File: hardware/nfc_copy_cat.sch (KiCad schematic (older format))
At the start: 28 parts, among them J1 USB_B_Micro, J2 Screw_Terminal_01x02, J3 Conn_02x02_Counter_Clockwise, J4 Conn_01x08, J5 Conn_01x02, J6 Conn_01x04, SW1 SW_DPST_x2, SW2 SW_DPST_x2, SW3 SW_DPST_x2, U1 AP2112K-3.3TRG1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

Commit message: añadimiento de led
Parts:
- added D4: LED_Small, LED_SMD:LED_0805_2012Metric_Pad1.15x1.40mm_HandSolder, symbol Device:LED_Small
- added R4: 330, Resistor_SMD:R_0805_2012Metric_Pad1.15x1.40mm_HandSolder, symbol Device:R_Small
- C4: value 0.1UF -> 0.1uf
- C6, C7, C8: value C -> 10uf
- R2: value R -> 1k
- R3: value R -> 2.2k
- U1: symbol croketa:AP2112K-3.3TRG1 -> electroniccats:AP2112K-3.3TRG1
- renumbered c1 to C1, c3 to C3
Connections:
- net labels added: 2(LED)
- wire segments 75 -> 78
- no-connect marks 21 -> 20
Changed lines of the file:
@@
 EESchema Schematic File Version 4
-LIBS:placa inventors house 1-cache
+LIBS:nfc_copy_cat-cache
 EELAYER 29 0
 EELAYER END
@@
 P 10800 1230
 F 0 "C4" H 10892 1276 50  0000 L CNN
-F 1 "0.1UF" H 10892 1185 50  0000 L CNN
+F 1 "0.1uf" H 10892 1185 50  0000 L CNN
 F 2 "Capacitor_SMD:C_0805_2012Metric_Pad1.15x1.40mm_HandSolder" H 10800 1230 50  0001 C CNN
 F 3 "~" H 10800 1230 50  0001 C CNN
@@
 	4950 1920 4950 1970
 $Comp
-L Device:C_Small c3
+L Device:C_Small C3
 U 1 1 5D106941
 P 4250 2070
-F 0 "c3" H 4342 2116 50  0000 L CNN
+F 0 "C3" H 4342 2116 50  0000 L CNN
 F 1 "0.1uf" H 4342 2025 50  0000 L CNN
 F 2 "Capacitor_SMD:C_0805_2012Metric_Pad1.15x1.40mm_HandSolder" H 4250 2070 50  0001 C CNN
@@
 $EndComp
 $Comp
-L Device:C_Small c1
+L Device:C_Small C1
 U 1 1 5D1030E9
 P 4950 2070
-F 0 "c1" H 5042 2116 50  0000 L CNN
+F 0 "C1" H 5042 2116 50  0000 L CNN
 F 1 "0.1uf" H 5042 2025 50  0000 L CNN
 F 2 "Capacitor_SMD:C_0805_2012Metric_Pad1.15x1.40mm_HandSolder" H 4950 2070 50  0001 C CNN
@@
 P 2310 3560
 F 0 "R2" H 2380 3606 50  0000 L CNN
-F 1 "R" H 2380 3515 50  0000 L CNN
+F 1 "1k" H 2380 3515 50  0000 L CNN
 F 2 "Resistor_SMD:R_0805_2012Metric_Pad1.15x1.40mm_HandSolder" V 2240 3560 50  0001 C CNN
 F 3 "~" H 2310 3560 50  0001 C CNN
@@
 P 1150 4020
 F 0 "R3" V 1357 4020 50  0000 C CNN
-F 1 "R" V 1266 4020 50  0000 C CNN
+F 1 "2.2k" V 1266 4020 50  0000 C CNN
 F 2 "Resistor_SMD:R_0805_2012Metric_Pad1.15x1.40mm_HandSolder" V 1080 4020 50  0001 C CNN
 F 3 "~" H 1150 4020 50  0001 C CNN
@@
 P 2180 4400
 F 0 "C7" H 2295 4446 50  0000 L CNN
-F 1 "C" H 2295 4355 50  0000 L CNN
+F 1 "10uf" H 2295 4355 50  0000 L CNN
 F 2 "Capacitor_SMD:C_0805_2012Metric_Pad1.15x1.40mm_HandSolder" H 2218 4250 50  0001 C CNN
 F 3 "~" H 2180 4400 50  0001 C CNN
@@
 P 910 3550
 F 0 "C8" H 1025 3596 50  0000 L CNN
-F 1 "C" H 1025 3505 50  0000 L CNN
+F 1 "10uf" H 1025 3505 50  0000 L CNN
 F 2 "Capacitor_SMD:C_0805_2012Metric_Pad1.15x1.40mm_HandSolder" H 948 3400 50  0001 C CNN
 F 3 "~" H 910 3550 50  0001 C CNN
@@
 NoConn ~ 7500 3620
 NoConn ~ 7500 3720
-NoConn ~ 7500 2720
 NoConn ~ 7500 2820
 NoConn ~ 10380 2480
@@
 $EndComp
 $Comp
-L croketa:AP2112K-3.3TRG1 U1
+L electroniccats:AP2112K-3.3TRG1 U1
 U 1 1 5D11FC1B
 P 1690 2450
@@
 P 2440 2400
 F 0 "C6" H 2555 2446 50  0000 L CNN
-F 1 "C" H 2555 2355 50  0000 L CNN
+F 1 "10uf" H 2555 2355 50  0000 L CNN
 F 2 "Capacitor_SMD:C_0805_2012Metric_Pad1.15x1.40mm_HandSolder" H 2478 2250 50  0001 C CNN
 F 3 "~" H 2440 2400 50  0001 C CNN
@@
 NoConn ~ 10320 4520
 NoConn ~ 10320 4420
+Wire Bus Line
+	3300 1830 3930 1830
+Wire Bus Line
+	3930 1830 3930 470
+$Comp
+L Device:LED_Small D4
+U 1 1 5D36129D
+P 3720 1220
+F 0 "D4" V 3766 1152 50  0000 R CNN
+F 1 "LED_Small" V 3675 1152 50  0000 R CNN
+F 2 "LED_SMD:LED_0805_2012Metric_Pad1.15x1.40mm_HandSolder" V 3720 1220 50  0001 C CNN
+F 3 "~" V 3720 1220 50  0001 C CNN
+	1    3720 1220
+	0    1    1    0
+$EndComp
+$Comp
+L Device:R_Small R4
+U 1 1 5D3612A3
+P 3720 970
+F 0 "R4" H 3779 1016 50  0000 L CNN
+F 1 "330" H 3779 925 50  0000 L CNN
+F 2 "Resistor_SMD:R_0805_2012Metric_Pad1.15x1.40mm_HandSolder" H 3720 970 50  0001 C CNN
+F 3 "~" H 3720 970 50  0001 C CNN
+	1    3720 970
+	-1   0    0    1
+$EndComp
+$Comp
+L MagSpoofTC-cache:GND #PWR026
+U 1 1 5D3612A9
+P 3720 820
+F 0 "#PWR026" H 3720 570 50  0001 C CNN
+F 1 "GND" H 3725 647 50  0000 C CNN
+F 2 "" H 3720 820 50  0000 C CNN
+F 3 "" H 3720 820 50  0000 C CNN
+	1    3720 820
+	-1   0    0    1
+$EndComp
+Wire Wire Line
+	3720 1370 3720 1320
+Wire Wire Line
+	3720 1120 3720 1070
+Wire Wire Line
+	3720 870  3720 820
+Text Label 7500 2720 0    50   ~ 0
+2(LED)
+Text Label 3720 1370 2    50   ~ 0
+2(LED)
 $EndSCHEMATC

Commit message: update schematic
new connector swd, fix cap vddcore, add leds
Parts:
- removed C3: 0.1uf, Capacitor_SMD:C_0805_2012Metric_Pad1.15x1.40mm_HandSolder, symbol Device:C_Small
- removed J3: Conn_02x02_Counter_Clockwise, Connector_PinHeader_2.54mm:PinHeader_2x02_P2.54mm_Vertical_SMD, symbol Connector_Generic:Conn_02x02_Counter_Clockwise
- removed J6: Conn_01x04, Connector_PinHeader_2.54mm:PinHeader_1x04_P2.54mm_Vertical, symbol Connector_Generic:Conn_01x04
- added D5, D6: LED, LED_SMD:LED_0805_2012Metric_Pad1.15x1.40mm_HandSolder, symbol Device:LED_Small
- added J3: SWD, symbol Connector:Conn_01x04_Male
- added R5, R6: 330, Resistor_SMD:R_0805_2012Metric_Pad1.15x1.40mm_HandSolder, symbol Device:R_Small
- D1: value LED_Small -> POWER
- D2: value D_Schottky -> MBR120
- D4: value LED_Small -> LED
- J2: value Screw_Terminal_01x02 -> Battery
- SW1: value SW_DPST_x2 -> RST; symbol Switch:SW_DPST_x2 -> nfc_copy_cat-rescue:SW_DPST_x2-Switch
- SW2: value SW_DPST_x2 -> Magspoof; symbol Switch:SW_DPST_x2 -> nfc_copy_cat-rescue:SW_DPST_x2-Switch
- SW3: value SW_DPST_x2 -> NFC; symbol Switch:SW_DPST_x2 -> nfc_copy_cat-rescue:SW_DPST_x2-Switch
- U3: symbol MagSpoofTC-cache:TC4424 -> nfc_copy_cat-rescue:TC4424-MagSpoofTC-cache
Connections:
- net labels added: +BATT, LED1, LED2, LED3
- net labels removed: 2(LED)
- wire segments 78 -> 81
- no-connect marks 20 -> 14
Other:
- note added: "COIL"
- note added: "MICROCONTROLLER"
- note added: "NFC CONNECTOR"
- note added: "SOURCE AND CHARGER"
- moved on the sheet: C1, C2, C4, C5, C6, D1, D2, D4, J2, J4, J5, R1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

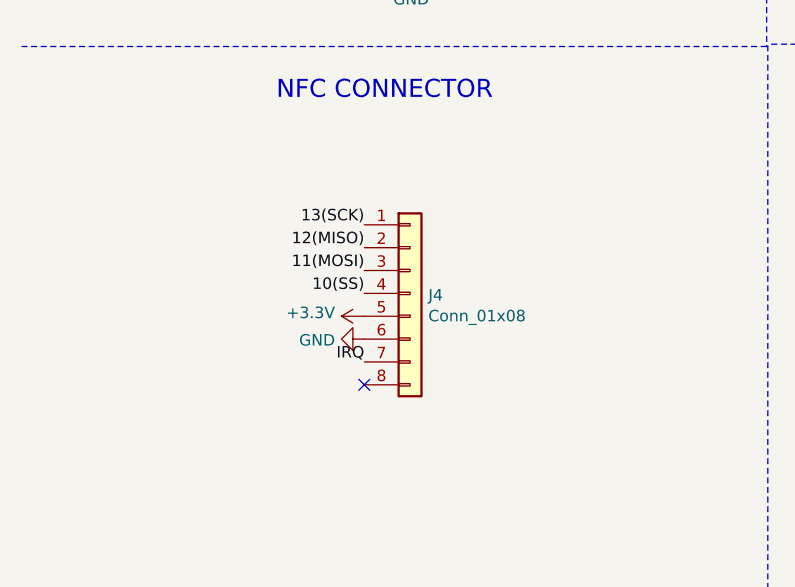
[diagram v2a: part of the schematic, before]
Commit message: add connector adafruit NFC
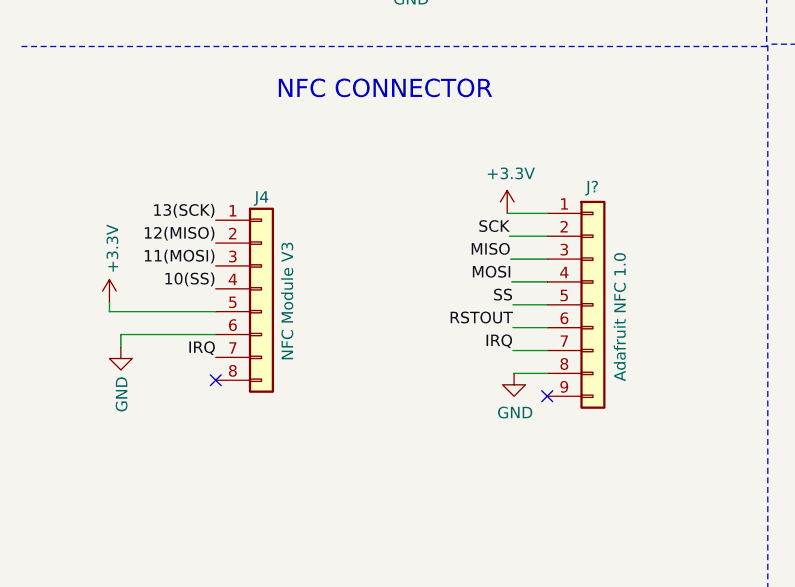
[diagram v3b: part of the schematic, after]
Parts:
- added J?: Adafruit NFC 1.0, symbol Connector_Generic:Conn_01x09
- J4: value Conn_01x08 -> NFC Module V3
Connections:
- net labels added: MISO, MOSI, RSTOUT, SCK, SS
- wire segments 81 -> 93
- no-connect marks 14 -> 15
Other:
- moved on the sheet: J4
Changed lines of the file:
@@
 L Connector_Generic:Conn_01x08 J4
 U 1 1 5D10E2FA
-P 2180 6010
-F 0 "J4" H 2260 6002 50  0000 L CNN
-F 1 "Conn_01x08" H 2260 5911 50  0000 L CNN
-F 2 "Connector_PinHeader_2.54mm:PinHeader_1x08_P2.54mm_Vertical" H 2180 6010 50  0001 C CNN
-F 3 "~" H 2180 6010 50  0001 C CNN
-	1    2180 6010
-	1    0    0    -1
-$EndComp
-Text Label 1980 5710 2    50   ~ 0
+P 1530 5990
+F 0 "J4" H 1500 6390 50  0000 L CNN
+F 1 "NFC Module V3" V 1645 5675 50  0000 L CNN
+F 2 "Connector_PinHeader_2.54mm:PinHeader_1x08_P2.54mm_Vertical" H 1530 5990 50  0001 C CNN
+F 3 "~" H 1530 5990 50  0001 C CNN
+	1    1530 5990
+	1    0    0    -1
+$EndComp
+Text Label 1330 5690 2    50   ~ 0
 13(SCK)
-Text Label 1980 5810 2    50   ~ 0
+Text Label 1330 5790 2    50   ~ 0
 12(MISO)
-Text Label 1980 5910 2    50   ~ 0
+Text Label 1330 5890 2    50   ~ 0
 11(MOSI)
-Text Label 1980 6010 2    50   ~ 0
+Text Label 1330 5990 2    50   ~ 0
 10(SS)
 $Comp
 L nfc_copy_cat-rescue:GND-MagSpoofTC-cache #PWR014
 U 1 1 5D111E6A
-P 1980 6210
-F 0 "#PWR014" H 1980 5960 50  0001 C CNN
-F 1 "GND" V 1985 6082 50  0000 R CNN
-F 2 "" H 1980 6210 50  0000 C CNN
-F 3 "" H 1980 6210 50  0000 C CNN
-	1    1980 6210
-	0    1    1    0
-$EndComp
-Text Label 1980 6310 2    50   ~ 0
+P 915 6245
+F 0 "#PWR014" H 915 5995 50  0001 C CNN
+F 1 "GND" V 920 6117 50  0000 R CNN
+F 2 "" H 915 6245 50  0000 C CNN
+F 3 "" H 915 6245 50  0000 C CNN
+	1    915  6245
+	1    0    0    -1
+$EndComp
+Text Label 1330 6290 2    50   ~ 0
 IRQ
 Text Label 10320 2270 0    50   ~ 0
@@
 NoConn ~ 7500 3720
 NoConn ~ 7500 2820
-NoConn ~ 1980 6410
+NoConn ~ 1330 6390
 NoConn ~ 10320 2120
 NoConn ~ 9320 2120
@@
 L power:+3.3V #PWR013
 U 1 1 5D1101C2
-P 1980 6110
-F 0 "#PWR013" H 1980 5960 50  0001 C CNN
-F 1 "+3.3V" V 1995 6238 50  0000 L CNN
-F 2 "" H 1980 6110 50  0001 C CNN
-F 3 "" H 1980 6110 50  0001 C CNN
-	1    1980 6110
-	0    -1   -1   0
+P 865 6050
+F 0 "#PWR013" H 865 5900 50  0001 C CNN
+F 1 "+3.3V" V 880 6178 50  0000 L CNN
+F 2 "" H 865 6050 50  0001 C CNN
+F 3 "" H 865 6050 50  0001 C CNN
+	1    865  6050
+	1    0    0    -1
 $EndComp
 Wire Wire Line
@@
 	4870 1510 4870 1440
 Connection ~ 4870 1510
+$Comp
+L Connector_Generic:Conn_01x09 J?
+U 1 1 5DBA44BD
+P 2980 6060
+F 0 "J?" H 2950 6575 50  0000 L CNN
+F 1 "Adafruit NFC 1.0" V 3100 5725 50  0000 L CNN
+F 2 "" H 2980 6060 50  0001 C CNN
+F 3 "~" H 2980 6060 50  0001 C CNN
+	1    2980 6060
+	1    0    0    -1
+$EndComp
+Wire Wire Line
+	2780 5660 2605 5660
+Wire Wire Line
+	2780 5760 2615 5760
+Wire Wire Line
+	2780 5860 2620 5860
+Wire Wire Line
+	2780 5960 2625 5960
+Wire Wire Line
+	2780 6060 2630 6060
+Wire Wire Line
+	2780 6160 2630 6160
+Wire Wire Line
+	2780 6260 2630 6260
+Wire Wire Line
+	2780 6360 2635 6360
+Text Label 2615 5760 2    50   ~ 0
+SCK
+Text Label 2620 5860 2    50   ~ 0
+MISO
+Text Label 2630 6060 2    50   ~ 0
+SS
+Text Label 2630 6160 2    50   ~ 0
+RSTOUT
+Text Label 2630 6260 2    50   ~ 0
+IRQ
+Text Label 2625 5960 2    50   ~ 0
+MOSI
+NoConn ~ 2780 6460
+$Comp
+L power:+3.3V #PWR?
+U 1 1 5DBC5E82
+P 2605 5660
+F 0 "#PWR?" H 2605 5510 50  0001 C CNN
+F 1 "+3.3V" H 2620 5833 50  0000 C CNN
+F 2 "" H 2605 5660 50  0001 C CNN
+F 3 "" H 2605 5660 50  0001 C CNN
+	1    2605 5660
+	1    0    0    -1
+$EndComp
+$Comp
+L power:GND #PWR?
+U 1 1 5DBC73AB
+P 2635 6360
+F 0 "#PWR?" H 2635 6110 50  0001 C CNN
+F 1 "GND" H 2640 6187 50  0000 C CNN
+F 2 "" H 2635 6360 50  0001 C CNN
+F 3 "" H 2635 6360 50  0001 C CNN
+	1    2635 6360
+	1    0    0    -1
+$EndComp
+Wire Wire Line
+	1330 6090 865  6090
+Wire Wire Line
+	865  6090 865  6050
+Wire Wire Line
+	1330 6190 915  6190
+Wire Wire Line
+	915  6190 915  6245
 $EndSCHEMATC

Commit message: Update traces, USB port and version 1.3v
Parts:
- J1: footprint Connectors_EC:629105150521 -> Connectors:U254051N4BH806
- U4: symbol electroniccats:ATSAMD21E18A -> nfc_copy_cat-rescue:ATSAMD21E18A-electroniccats
- gave numbers to parts that had none: 1
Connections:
- net labels removed: BAT
- wire segments 93 -> 96
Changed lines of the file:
@@
 EESchema Schematic File Version 4
 LIBS:nfc_copy_cat-cache
-EELAYER 30 0
+EELAYER 29 0
 EELAYER END
 $Descr A4 11693 8268
@@
 Sheet 1 1
 Title "NFC Copy Cat"
-Date "2019-10-30"
-Rev "1.1v"
-Comp "electronic cats"
+Date "2019-11-15"
+Rev "1.2v"
+Comp "Electronic Cats"
 Comment1 ""
-Comment2 ""
+Comment2 "Eduardo Contreras"
 Comment3 "Andres Sabas"
 Comment4 "Juan Eduardo Rangel Macias "
@@
 F 0 "J1" H 937 1547 50  0000 C CNN
 F 1 "USB_B_Micro" H 937 1456 50  0000 C CNN
-F 2 "Connectors_EC:629105150521" H 1030 1030 50  0001 C CNN
+F 2 "Connectors:U254051N4BH806" H 1030 1030 50  0001 C CNN
 F 3 "~" H 1030 1030 50  0001 C CNN
 	1    880  1080
@@
 	2100 3820 2180 3820
 Wire Wire Line
-	2180 3820 2180 4250
-Text Label 2180 4170 0    50   ~ 0
-BAT
+	2180 3820 2180 4175
 Wire Wire Line
 	1700 3410 1520 3410
@@
 	7500 1720 7550 1720
 $Comp
-L electroniccats:ATSAMD21E18A U4
+L nfc_copy_cat-rescue:ATSAMD21E18A-electroniccats U4
 U 1 1 5D120B36
 P 6100 2720
@@
 Connection ~ 4870 1510
 $Comp
-L Connector_Generic:Conn_01x09 J?
+L Connector_Generic:Conn_01x09 J6
 U 1 1 5DBA44BD
 P 2980 6060
-F 0 "J?" H 2950 6575 50  0000 L CNN
+F 0 "J6" H 2950 6575 50  0000 L CNN
 F 1 "Adafruit NFC 1.0" V 3100 5725 50  0000 L CNN
 F 2 "" H 2980 6060 50  0001 C CNN
@@
 NoConn ~ 2780 6460
 $Comp
-L power:+3.3V #PWR?
+L power:+3.3V #PWR0101
 U 1 1 5DBC5E82
 P 2605 5660
-F 0 "#PWR?" H 2605 5510 50  0001 C CNN
+F 0 "#PWR0101" H 2605 5510 50  0001 C CNN
 F 1 "+3.3V" H 2620 5833 50  0000 C CNN
 F 2 "" H 2605 5660 50  0001 C CNN
@@
 $EndComp
 $Comp
-L power:GND #PWR?
+L power:GND #PWR0102
 U 1 1 5DBC73AB
 P 2635 6360
-F 0 "#PWR?" H 2635 6110 50  0001 C CNN
+F 0 "#PWR0102" H 2635 6110 50  0001 C CNN
 F 1 "GND" H 2640 6187 50  0000 C CNN
 F 2 "" H 2635 6360 50  0001 C CNN
@@
 Wire Wire Line
 	915  6190 915  6245
+$Comp
+L power:+BATT #PWR0103
+U 1 1 5DD5BE11
+P 2620 4140
+F 0 "#PWR0103" H 2620 3990 50  0001 C CNN
+F 1 "+BATT" H 2635 4313 50  0000 C CNN
+F 2 "" H 2620 4140 50  0001 C CNN
+F 3 "" H 2620 4140 50  0001 C CNN
+	1    2620 4140
+	1    0    0    -1
+$EndComp
+Wire Wire Line
+	2620 4140 2620 4175
+Wire Wire Line
+	2620 4175 2180 4175
+Connection ~ 2180 4175
+Wire Wire Line
+	2180 4175 2180 4250
 $EndSCHEMATC

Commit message: nfc board v3
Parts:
- J6: footprint (none) -> Connector_PinHeader_2.54mm:PinHeader_1x09_P2.54mm_Vertical
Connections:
- net MISO is gone; now on net IRQ: J6.3 (Pin_3)
- net MOSI is gone; now on net RSTOUT: J6.4 (Pin_4)
- net SCK is gone; now on net GND: J6.2 (Pin_2)
- net SS is gone; now on net 10(SS): J6.5 (Pin_5)
- net +3V3: now also J6.9 (Pin_9); no longer J6.1 (Pin_1)
- net 11(MOSI): now also J6.6 (Pin_6)
- net 12(MISO): now also J6.7 (Pin_7)
- net 13(SCK): now also J6.8 (Pin_8)
- net GND: no longer J6.8 (Pin_8)
- net IRQ: no longer J6.7 (Pin_7)
- net RSTOUT: no longer J6.6 (Pin_6)

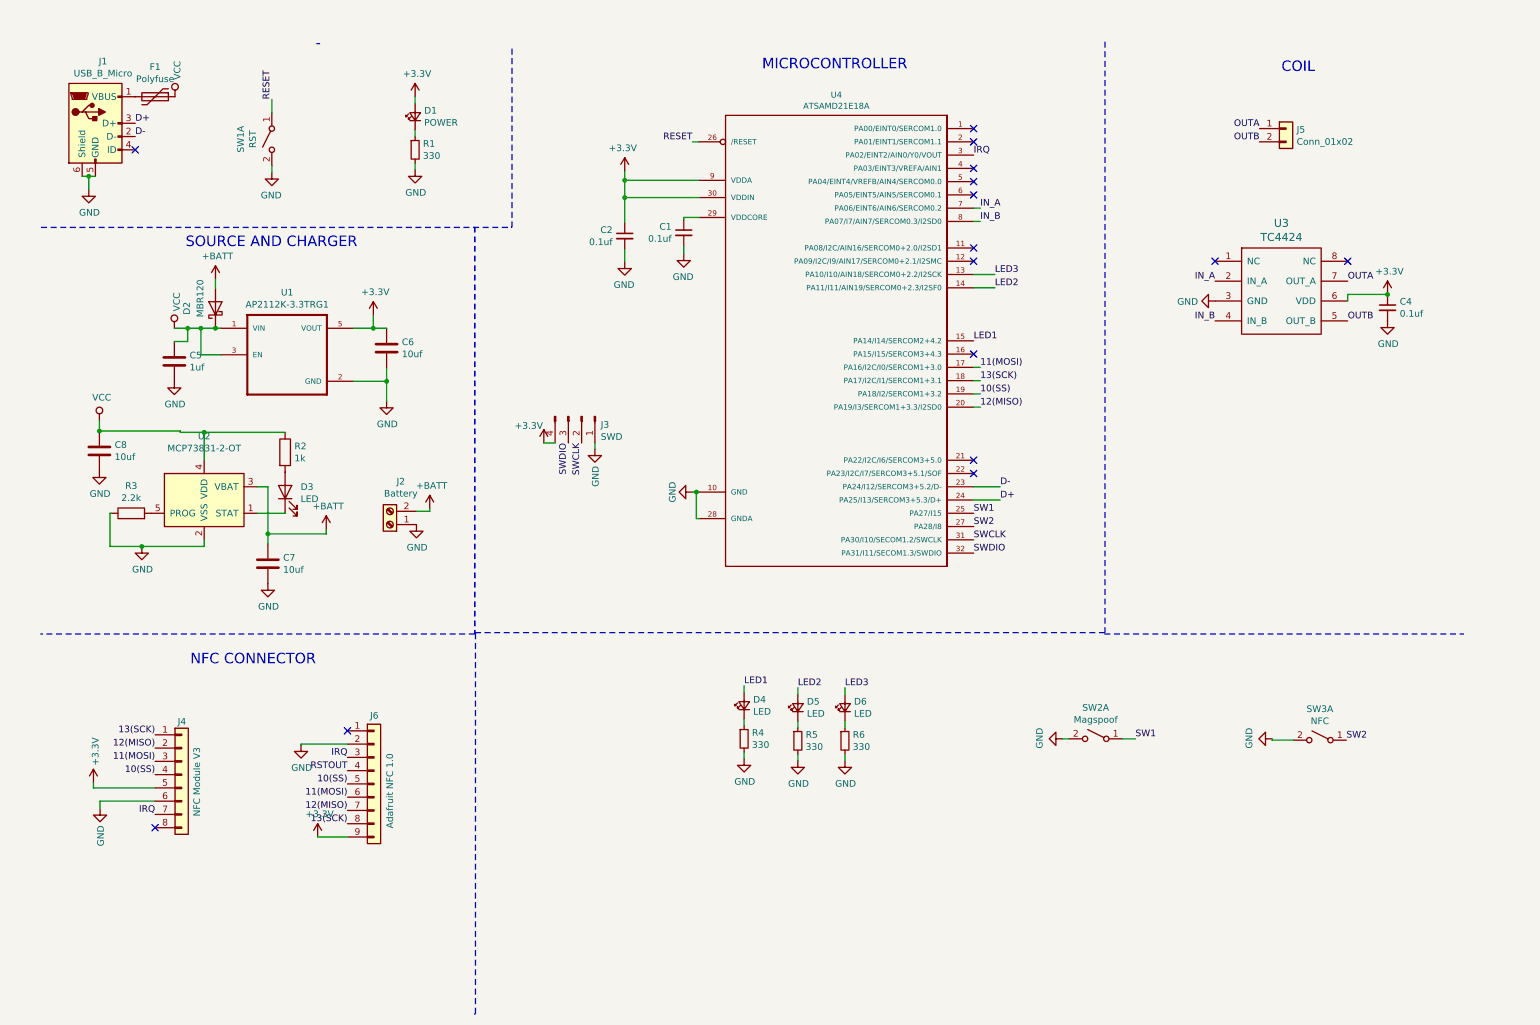
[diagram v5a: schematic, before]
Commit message: spi flash
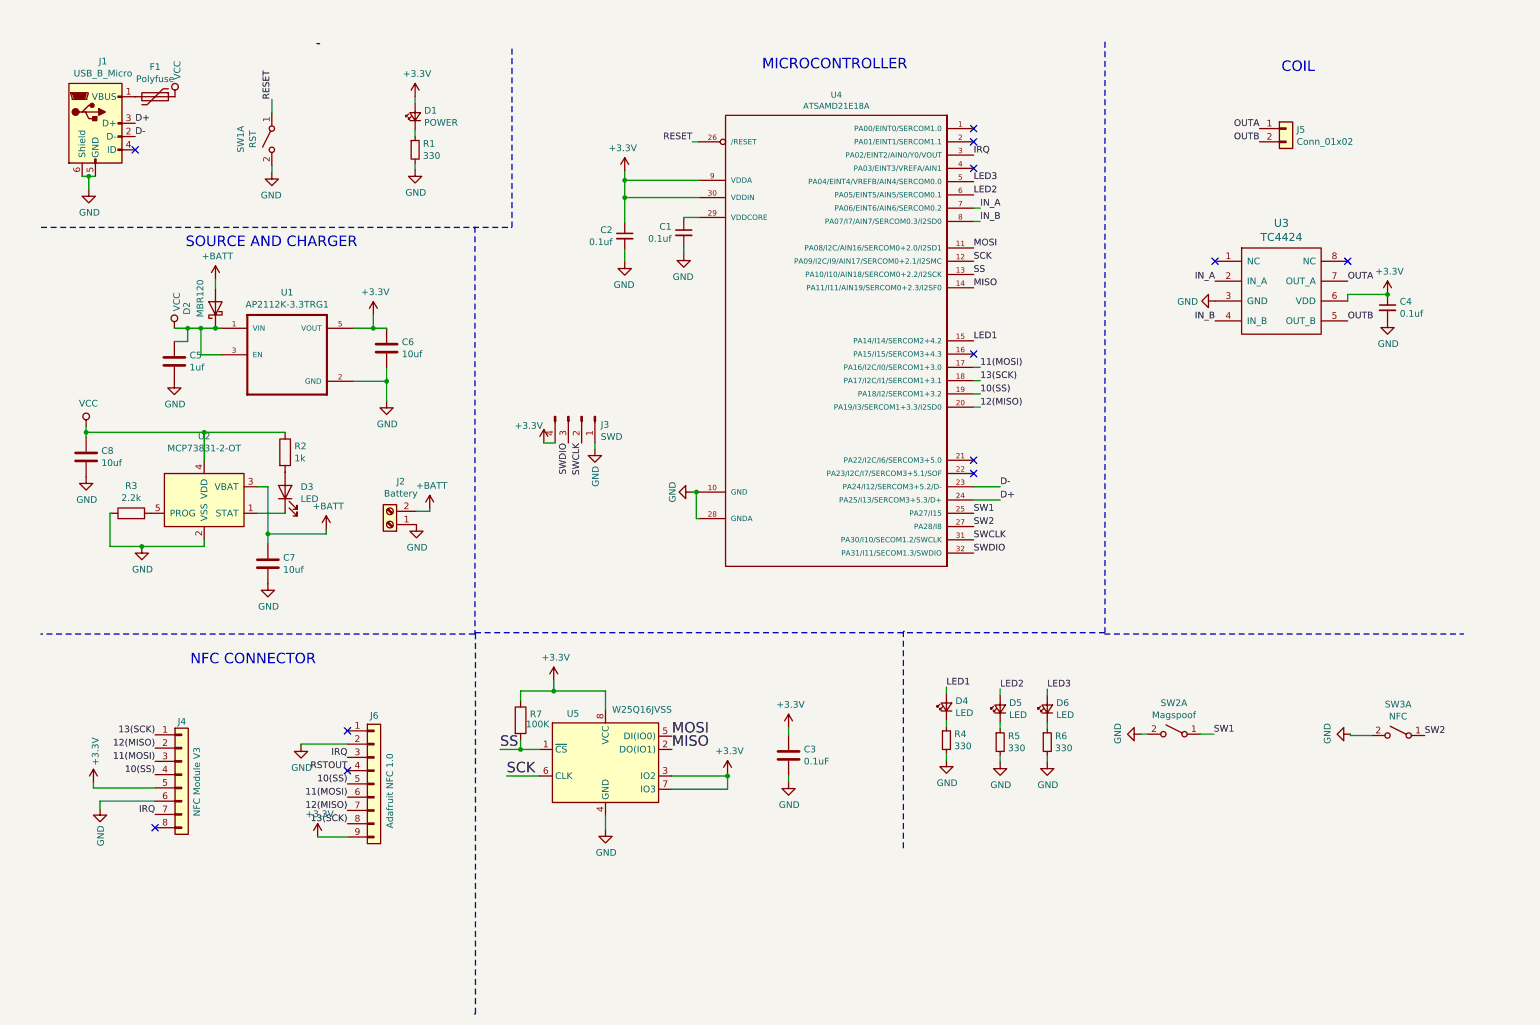
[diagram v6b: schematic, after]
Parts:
- added C3: 0.1uF, symbol Device:C
- added R7: 100K, symbol Device:R
- added U5: W25Q16JVSS, Package_SO:SOIC-8_5.23x5.23mm_P1.27mm, symbol Memory_Flash:W25Q32JVSS
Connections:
- net +3V3: now also C3.1, R7.1, U5.3 (IO2), U5.7 (IO3), U5.8 (VCC)
- net GND: now also C3.2, U5.4 (GND)
- net LED2: now also U4.6 (PA05/EINT5/AIN5/SERCOM0.1); no longer U4.14 (PA11/I11/AIN19/SERCOM0+2.3/I2SF0)
- net LED3: now also U4.5 (PA04/EINT4/VREFB/AIN4/SERCOM0.0); no longer U4.13 (PA10/I10/AIN18/SERCOM0+2.2/I2SCK)
- net MOSI: now reaches U4.11 (PA08/I2C/AIN16/SERCOM0+2.0/I2SD1)
- net MOSI: now also U5.5 (DI(IO0))
- net SCK: now reaches U4.12 (PA09/I2C/I9/AIN17/SERCOM0+2.1/I2SMC)
- net SCK: now also U5.6 (CLK)
- new net MISO: U4.14 (PA11/I11/AIN19/SERCOM0+2.3/I2SF0), U5.2 (DO(IO1))
- new net SS: R7.2, U4.13 (PA10/I10/AIN18/SERCOM0+2.2/I2SCK), U5.1 (~CS)
- no-connect marks 15 -> 12
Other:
- moved on the sheet: C8, D4, D5, D6, R4, R5, R6, SW2A, SW3A
